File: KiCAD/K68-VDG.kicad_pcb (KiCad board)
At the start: 2 copper layers, 100 x 75 mm, 48 parts, among them J1 Video Out, J2 SBC6303 BUS, Q1 2SA1015, Q2 2SC1815, U1 MC6847, U10 74LS138, U2 MC1372, U3 74LS32, U4 74HCT573, U5 74LS02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

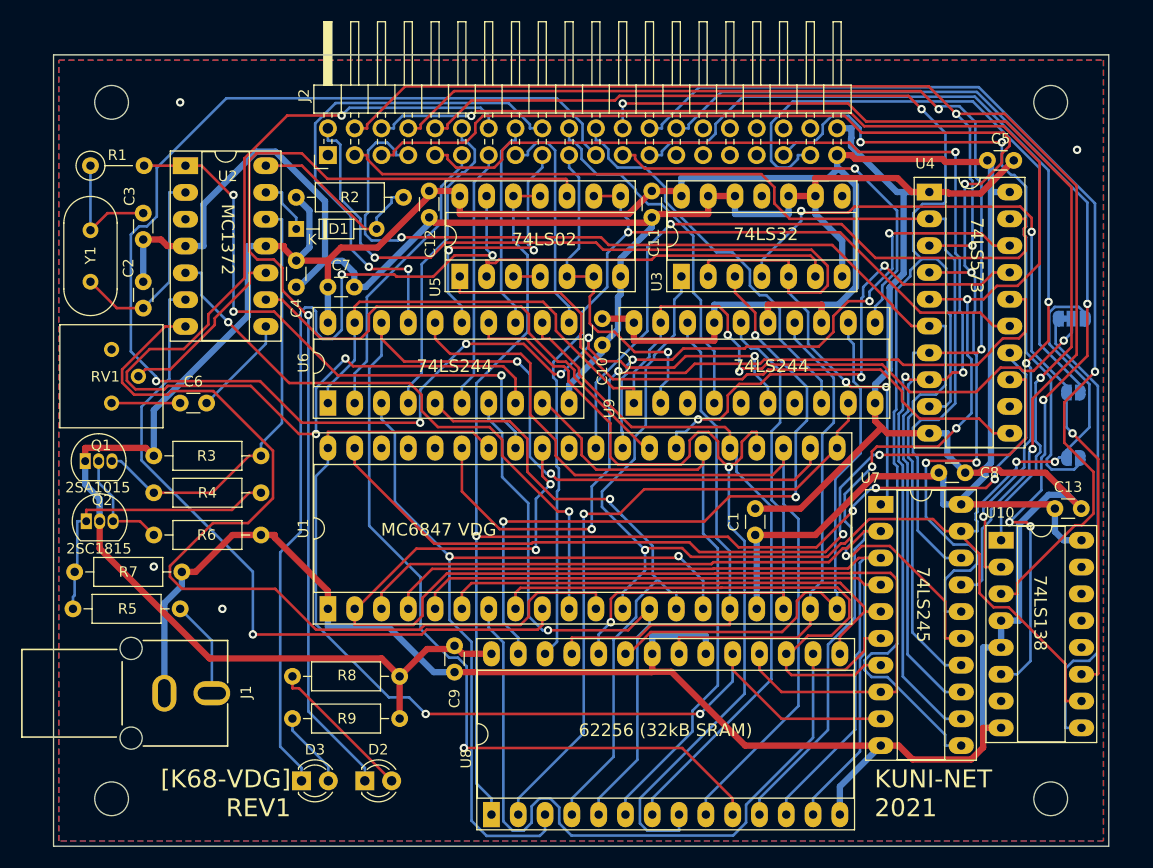
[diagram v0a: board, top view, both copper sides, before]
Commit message: REV1.1 バグ修正板 ガーバー出力
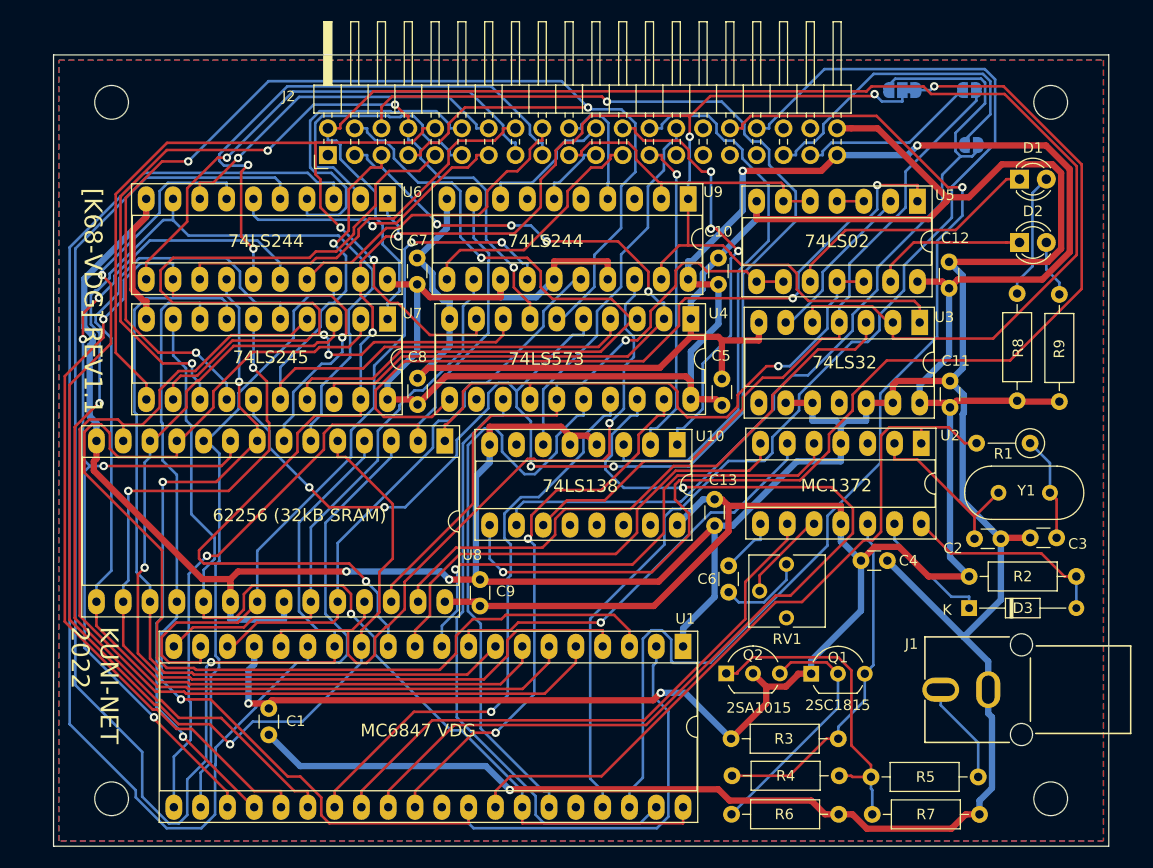
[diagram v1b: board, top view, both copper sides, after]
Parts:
- D1: value 1N4007 -> A13_LED; footprint Diode_THT:D_DO-34_SOD68_P7.62mm_Horizontal -> LED_THT:LED_D3.0mm
- D2: value LED_A13 -> A14_LED
- D3: value LED_A14 -> 1N4007; footprint LED_THT:LED_D3.0mm -> Diode_THT:D_DO-34_SOD68_P10.16mm_Horizontal
- JP1: value 8000-JP -> VRAM-JP; footprint Jumper:SolderJumper-2_P1.3mm_Open_RoundedPad1.0x1.5mm -> Jumper:SolderJumper-3_P1.3mm_Bridged12_RoundedPad1.0x1.5mm
- JP2: value A000-JP -> 8000-JP
- JP3: value VRAM JP -> A000-JP; footprint Jumper:SolderJumper-3_P1.3mm_Bridged12_RoundedPad1.0x1.5mm -> Jumper:SolderJumper-2_P1.3mm_Open_RoundedPad1.0x1.5mm
- Q1, Q2: footprint Package_TO_SOT_THT:TO-92_Inline -> Package_TO_SOT_THT:TO-92_Inline_Wide
- RV1: footprint Potentiometer_THT:Potentiometer_Bourns_3386P_Vertical -> Potentiometer_THT:Potentiometer_Vishay_T73YP_Vertical
- moved R1 92.9 mm to (232.6, 116.8), turned to 180 degrees
- moved C3 88.7 mm to (232.6, 125.8), turned to 0 degrees
- moved Y1 88.3 mm to (229.6, 121.5), turned to 0 degrees
- moved C2 84.9 mm to (229.8, 125.9), turned to 180 degrees
- moved D2 80.3 mm to (231.5, 97.8)
- moved R7 79.0 mm to (217.6, 152.0)
- moved J1 78.1 mm to (228.6, 140.2), turned to -90 degrees
- moved R5 77.3 mm to (227.6, 148.4)
- moved U2 74.5 mm to (222.2, 116.8), turned to -90 degrees
- moved R2 73.2 mm to (226.8, 129.4)
- moved Q1 71.7 mm to (211.8, 138.7)
- moved R9 69.4 mm to (235.3, 112.9), turned to 90 degrees
- moved D1 68.7 mm to (231.5, 91.8)
- moved RV1 65.8 mm to (209.5, 128.3), turned to 180 degrees
- moved D3 65.4 mm to (226.8, 132.4)
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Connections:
- net /~WR renamed /~{WR}
- D1 pad 1: Net-(D1-Pad1) -> Net-(U5-Pad10)
- D1 pad 2: Net-(D1-Pad2) -> Net-(R8-Pad2)
- D2 pad 1: Net-(D2-Pad1) -> Net-(U5-Pad13)
- D2 pad 2: Net-(D2-Pad2) -> Net-(R9-Pad2)
- D3 pad 1: Net-(D3-Pad1) -> Net-(U2-Pad13)
- D3 pad 2: Net-(D3-Pad2) -> Net-(R2-Pad2)
- J2 pad 1: (no net) -> /~{RD}
- J2 pad 27: (no net) -> /R~{W}
- J2 pad 29: (no net) -> /~{IRQ}
- J2 pad 30: (no net) -> /~{RES}
- J2 pad 31: (no net) -> /NMI
- J2 pad 32: (no net) -> /~{HS}
- J2 pad 33: (no net) -> /E000c
- J2 pad 34: (no net) -> /~{FS}
- J2 pad 36: (no net) -> /P15
- J2 pad 38: (no net) -> /P17
- JP1 pad 1: /8000 -> /C000
- JP1 pad 2: /8000c -> /MEMCS
- JP2 pad 1: /A000 -> /8000
- JP2 pad 2: /A000c -> /8000c
- JP3 pad 1: /C000 -> /A000
- JP3 pad 2: /VRAM_AD -> /A000c
- R2 pad 2: Net-(D1-Pad2) -> Net-(R2-Pad2)
- R8 pad 2: Net-(D2-Pad2) -> Net-(R8-Pad2)
- R9 pad 2: Net-(D3-Pad2) -> Net-(R9-Pad2)
- RV1 pad 3: (no net) -> unconnected-(RV1-Pad3)
- U1 pad 12: /A000 -> /MEMCS
- U1 pad 31: (no net) -> unconnected-(U1-Pad31)
- U1 pad 36: (no net) -> unconnected-(U1-Pad36)
- U1 pad 37: (no net) -> /~{FS}
- U1 pad 38: (no net) -> /~{HS}
- U10 pad 12: (no net) -> unconnected-(U10-Pad12)
- U10 pad 13: (no net) -> unconnected-(U10-Pad13)
- U10 pad 14: (no net) -> unconnected-(U10-Pad14)
- U10 pad 15: (no net) -> unconnected-(U10-Pad15)
- U10 pad 7: (no net) -> unconnected-(U10-Pad7)
- U2 pad 13: Net-(D1-Pad1) -> Net-(U2-Pad13)
- U2 pad 14: Net-(D1-Pad2) -> Net-(R2-Pad2)
- U2 pad 3: (no net) -> unconnected-(U2-Pad3)
- U3 pad 1: /A000 -> /MEMCS
- U3 pad 11: (no net) -> unconnected-(U3-Pad11)
- U3 pad 8: (no net) -> unconnected-(U3-Pad8)
- U4 pad 12: (no net) -> unconnected-(U4-Pad12)
- U5 pad 10: Net-(D2-Pad1) -> Net-(U5-Pad10)
- U5 pad 13: Net-(D3-Pad1) -> Net-(U5-Pad13)
- U6 pad 1: /VRAM_AD -> /MEMCS
- U6 pad 19: /VRAM_AD -> /MEMCS
- U7 pad 19: /A000 -> /MEMCS
- U9 pad 1: /VRAM_AD -> /MEMCS
- U9 pad 19: /VRAM_AD -> /MEMCS
- U9 pad 3: (no net) -> unconnected-(U9-Pad3)
- U9 pad 5: (no net) -> unconnected-(U9-Pad5)
- U9 pad 7: (no net) -> unconnected-(U9-Pad7)
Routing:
- net /MEMCS: track 0.00 -> 171.8 mm, vias 0 -> 5
- net /A10: track 143.8 -> 6.75 mm, vias 6 -> 0
- net /~{FS}: track 0.00 -> 114.2 mm
- net /~{HS}: track 0.00 -> 106.2 mm, vias 0 -> 1
- net GND: track 377.4 -> 480.7 mm, vias 4 -> 3
- net /VRAM_AD: track 102.0 -> 0.00 mm, vias 3 -> 0
- net Net-(D2-Pad1): track 97.3 -> 0.00 mm, vias 1 -> 0
- net Net-(D3-Pad1): track 79.2 -> 0.00 mm, vias 2 -> 0
- net /DA6: track 61.1 -> 137.2 mm
- net /DA14: track 130.7 -> 55.6 mm, vias 4 -> 1
- net /DA0: track 128.6 -> 58.2 mm, vias 3 -> 0
- net /A3: track 102.0 -> 33.7 mm, vias 3 -> 1
- net /C000: track 44.2 -> 108.2 mm, vias 0 -> 2
- net /DA7: track 80.2 -> 141.8 mm, vias 2 -> 0
- net /D1: track 134.6 -> 73.3 mm, vias 3 -> 1
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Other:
- net class BOLD removed
- net class Default removed
- board text added: "$C000:$A000"
- board text added: "KUNI-NET 2022"
- board text added: "[K68-VDG] REV1.1"
- board text removed: "$A000:$C000"
- board text removed: "KUNI-NET 2021"
- board text removed: "[K68-VDG] REV1"

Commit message: 基板シルク印刷間違い訂正、回路図C1間違い訂正、v1.2ガーバー出力
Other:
- board text added: "KUNI-NET 2023"
- board text added: "[K68-VDG] REV1.2"
- board text removed: "KUNI-NET 2022"
- board text removed: "[K68-VDG] REV1.1"
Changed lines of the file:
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@@
     (effects (font (size 1.2 1.2) (thickness 0.2)))
   )
-  (gr_text "KUNI-NET\n2022" (at 143.88 134.17 270) (layer "F.SilkS")
+  (gr_text "KUNI-NET\n2023" (at 143.88 134.17 270) (layer "F.SilkS")
     (effects (font (size 1.7 1.7) (thickness 0.3)) (justify left))
   )
@@
     (effects (font (size 1.2 1.2) (thickness 0.2)))
   )
-  (gr_text "[K68-VDG] REV1.1" (at 143.73 114.09 270) (layer "F.SilkS")
+  (gr_text "[K68-VDG] REV1.2" (at 143.73 114.09 270) (layer "F.SilkS")
     (effects (font (size 1.7 1.7) (thickness 0.3)) (justify right))
   )
-  (gr_text "2SA1015" (at 206.84 141.88) (layer "F.SilkS")
+  (gr_text "2SA1015" (at 214.5 141.5) (layer "F.SilkS")
     (effects (font (size 1 1) (thickness 0.15)))
   )
@@
     (effects (font (size 1.2 1.2) (thickness 0.2)))
   )
-  (gr_text "2SC1815" (at 214.32 141.63) (layer "F.SilkS")
+  (gr_text "2SC1815" (at 206 141.5) (layer "F.SilkS")
     (effects (font (size 1 1) (thickness 0.15)))
   )
